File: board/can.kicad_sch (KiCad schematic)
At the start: 21 parts, among them U4 ATA6561, U5 ATA6561, U6 ATA6561

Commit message: Changing CRX and CTX Round 2 :((
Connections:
- net CANRX7 renamed CANRX3
- net CANTX7 renamed CANTX3
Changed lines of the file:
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@@
 		)
 	)
-	(hierarchical_label "CANTX7"
+	(hierarchical_label "CANTX3"
 		(shape input)
 		(at 81.28 172.72 180)
@@
 		)
 	)
-	(hierarchical_label "CANRX7"
+	(hierarchical_label "CANRX3"
 		(shape output)
 		(at 81.28 175.26 180)

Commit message: Added root pins
Root beer
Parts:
- added C16, C17: 100nF, symbol Device:C
- added C18: 4.7nF, symbol Device:C
- added Conn5: Molex_SL_02, symbol MRDT_Connectors:Molex_SL_02
- added R24, R25: 60, symbol Device:R_US
- added U7: ATA6561, Package_SO:SOIC-8_3.9x4.9mm_P1.27mm, symbol MRDT_Devices:ATA6561
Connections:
- net +3.3V: now also C16.2, U7.5 (VIO)
- net +5V: now also C17.1, U7.3 (VCC)
- net CANRX1: now also U7.4 (RXD)
- net CANTX1: now also U7.1 (TXD)
- net GND: now also C16.1, C17.2, C18.2, U7.2 (GND), U7.8 (STBY)
- new net: C18.1, R24.2, R25.1
- new net: Conn5.2, R25.2, U7.6 (CANL)
- new net: Conn5.1, R24.1, U7.7 (CANH)

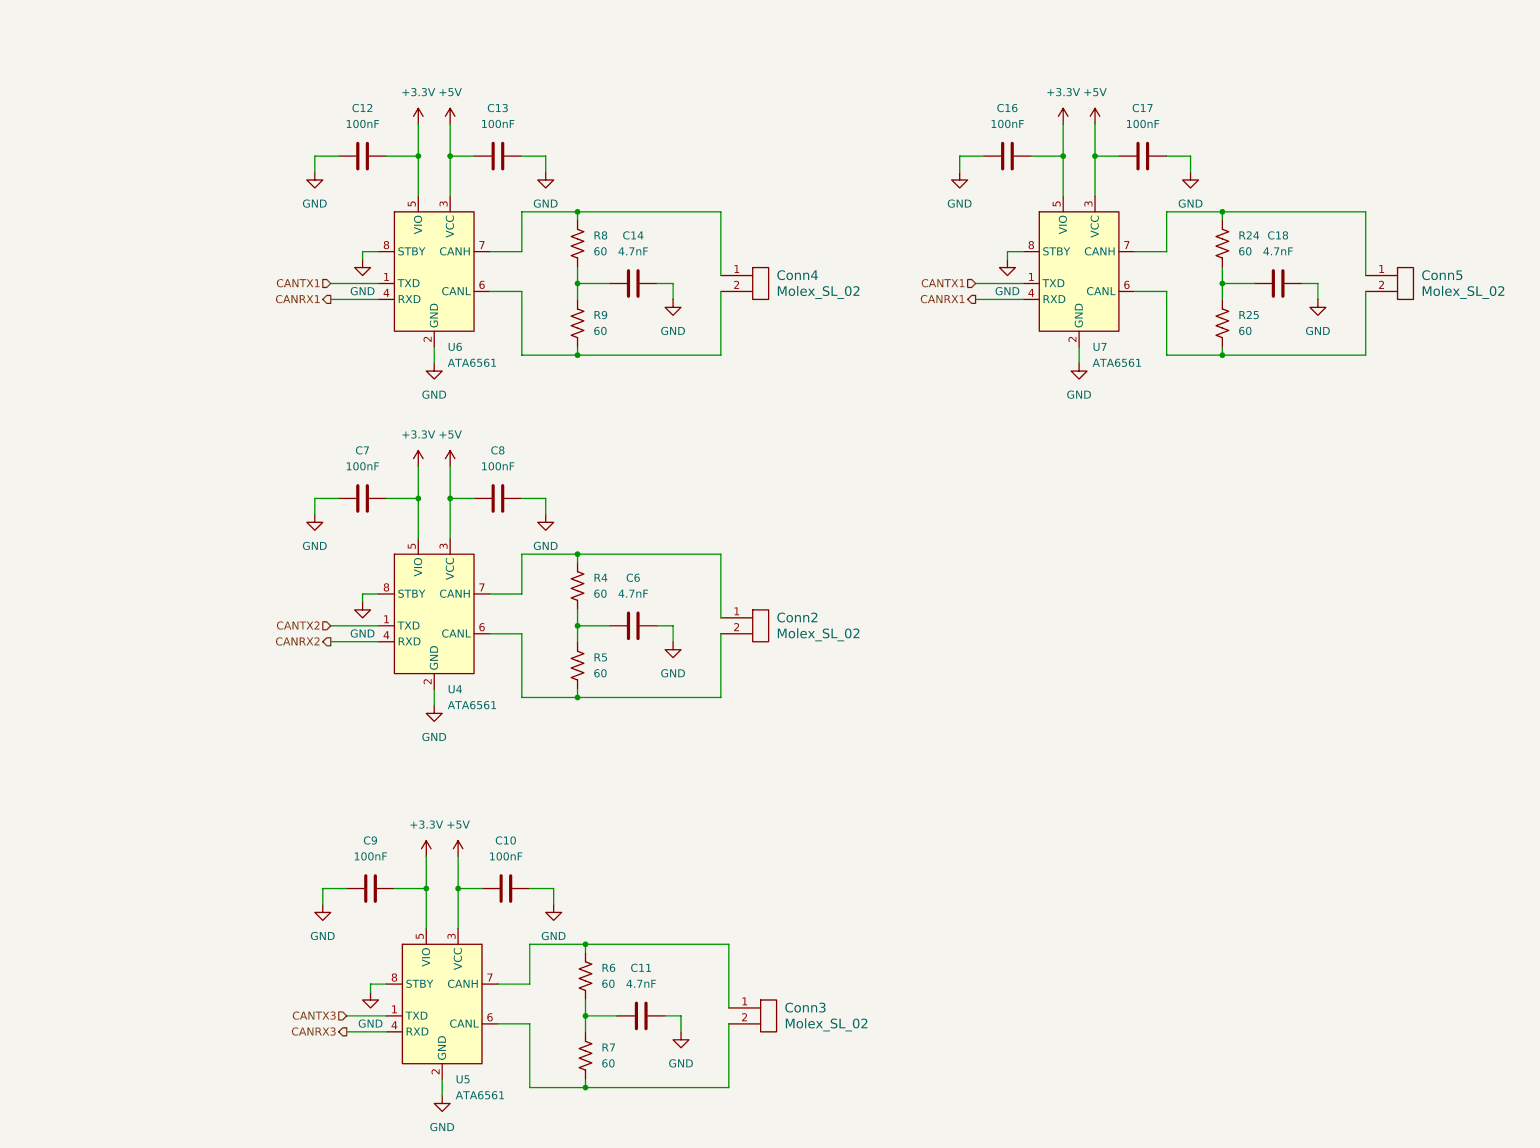
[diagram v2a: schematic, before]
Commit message: Schematic review changes
Updated molex connectors, can ics, buttons are no longer pull ups, and some appearence changes.
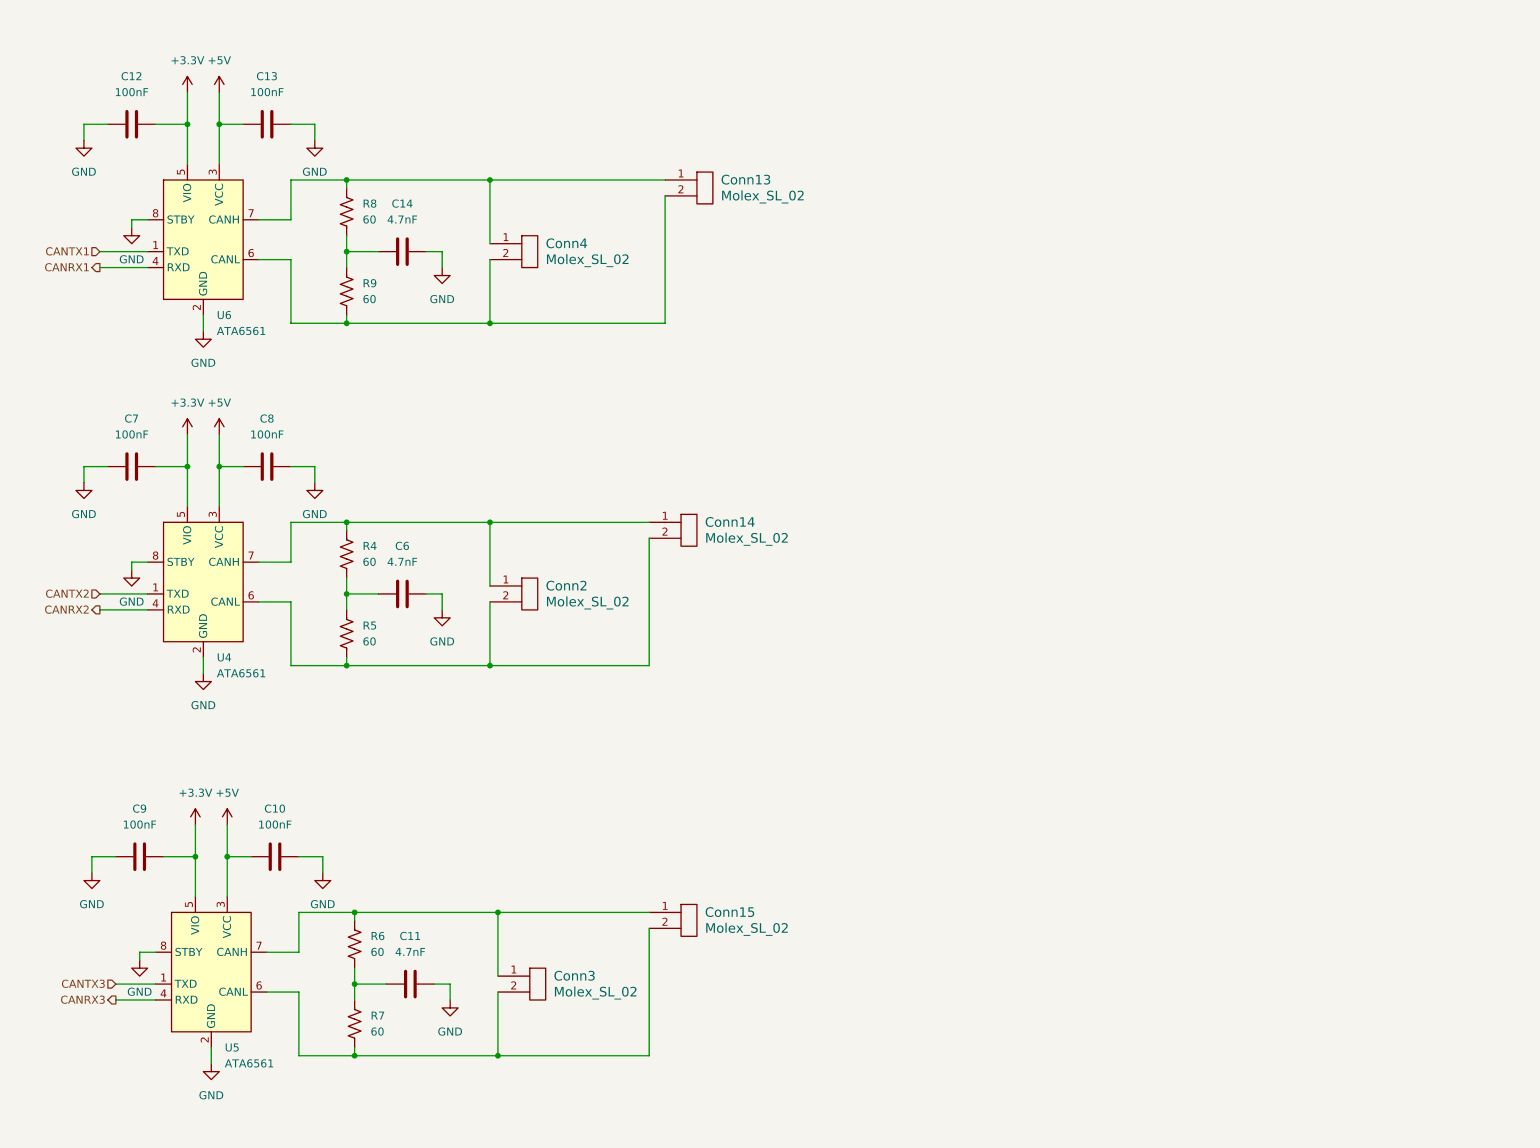
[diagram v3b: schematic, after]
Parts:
- removed C16, C17: 100nF, symbol Device:C
- removed C18: 4.7nF, symbol Device:C
- removed Conn5: Molex_SL_02, symbol MRDT_Connectors:Molex_SL_02
- removed R24, R25: 60, symbol Device:R_US
- removed U7: ATA6561, Package_SO:SOIC-8_3.9x4.9mm_P1.27mm, symbol MRDT_Devices:ATA6561
- added Conn13, Conn14, Conn15: Molex_SL_02, symbol MRDT_Connectors:Molex_SL_02
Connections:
- net at Conn4.2, R9.2, U6.6 (CANL): now also Conn13.2
- net at Conn2.1, R4.1, U4.7 (CANH): now also Conn14.1
- net at Conn2.2, R5.2, U4.6 (CANL): now also Conn14.2
- net at Conn4.1, R8.1, U6.7 (CANH): now also Conn13.1
- net at Conn3.1, R6.1, U5.7 (CANH): now also Conn15.1
- net at Conn3.2, R7.2, U5.6 (CANL): now also Conn15.2
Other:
- moved on the sheet: C10, C11, C12, C13, C14, C6, C7, C8, C9, Conn2, Conn3, Conn4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

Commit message: Prototype Layout
Made an initial Layout to be edited and changed uwu
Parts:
- C10, C11, C12, C13, C14, C6, C7, C8, C9: footprint (none) -> Capacitor_SMD:C_0603_1608Metric_Pad1.08x0.95mm_HandSolder
- Conn13, Conn14, Conn15, Conn2, Conn3, Conn4: footprint (none) -> MRDT_Connectors:MOLEX_SL_02_Vertical
- R4, R5, R6, R7, R8, R9: footprint (none) -> Resistor_SMD:R_0603_1608Metric_Pad0.98x0.95mm_HandSolder
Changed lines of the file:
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@@
 			)
 		)
-		(property "Footprint" ""
+		(property "Footprint" "Capacitor_SMD:C_0603_1608Metric_Pad1.08x0.95mm_HandSolder"
 			(at 73.66 146.3548 0)
 			(effects
@@
 			)
 		)
-		(property "Footprint" ""
+		(property "Footprint" "Resistor_SMD:R_0603_1608Metric_Pad0.98x0.95mm_HandSolder"
 			(at 82.296 57.404 90)
 			(effects
@@
 			)
 		)
-		(property "Footprint" ""
+		(property "Footprint" "Capacitor_SMD:C_0603_1608Metric_Pad1.08x0.95mm_HandSolder"
 			(at 72.39 84.1248 0)
 			(effects
@@
 			)
 		)
-		(property "Footprint" ""
+		(property "Footprint" "MRDT_Connectors:MOLEX_SL_02_Vertical"
 			(at 137.16 45.72 0)
 			(effects
@@
 			)
 		)
-		(property "Footprint" ""
+		(property "Footprint" "Resistor_SMD:R_0603_1608Metric_Pad0.98x0.95mm_HandSolder"
 			(at 82.296 99.314 90)
 			(effects
@@
 			)
 		)
-		(property "Footprint" ""
+		(property "Footprint" "MRDT_Connectors:MOLEX_SL_02_Vertical"
 			(at 109.22 110.49 0)
 			(effects
@@
 			)
 		)
-		(property "Footprint" ""
+		(property "Footprint" "Capacitor_SMD:C_0603_1608Metric_Pad1.08x0.95mm_HandSolder"
 			(at 93.98 49.8348 0)
 			(effects
@@
 			)
 		)
-		(property "Footprint" ""
+		(property "Footprint" "MRDT_Connectors:MOLEX_SL_02_Vertical"
 			(at 109.22 55.88 0)
 			(effects
@@
 			)
 		)
-		(property "Footprint" ""
+		(property "Footprint" "Capacitor_SMD:C_0603_1608Metric_Pad1.08x0.95mm_HandSolder"
 			(at 95.25 166.6748 0)
 			(effects
@@
 			)
 		)
-		(property "Footprint" ""
+		(property "Footprint" "Capacitor_SMD:C_0603_1608Metric_Pad1.08x0.95mm_HandSolder"
 			(at 52.07 146.3548 0)
 			(effects
@@
 			)
 		)
-		(property "Footprint" ""
+		(property "Footprint" "Capacitor_SMD:C_0603_1608Metric_Pad1.08x0.95mm_HandSolder"
 			(at 72.39 29.5148 0)
 			(effects
@@
 			)
 		)
-		(property "Footprint" ""
+		(property "Footprint" "Resistor_SMD:R_0603_1608Metric_Pad0.98x0.95mm_HandSolder"
 			(at 83.566 161.544 90)
 			(effects
@@
 			)
 		)
-		(property "Footprint" ""
+		(property "Footprint" "MRDT_Connectors:MOLEX_SL_02_Vertical"
 			(at 134.62 162.56 0)
 			(effects
@@
 			)
 		)
-		(property "Footprint" ""
+		(property "Footprint" "Resistor_SMD:R_0603_1608Metric_Pad0.98x0.95mm_HandSolder"
 			(at 82.296 44.704 90)
 			(effects
@@
 			)
 		)
-		(property "Footprint" ""
+		(property "Footprint" "Capacitor_SMD:C_0603_1608Metric_Pad1.08x0.95mm_HandSolder"
 			(at 50.8 29.5148 0)
 			(effects
@@
 			)
 		)
-		(property "Footprint" ""
+		(property "Footprint" "Capacitor_SMD:C_0603_1608Metric_Pad1.08x0.95mm_HandSolder"
 			(at 50.8 84.1248 0)
 			(effects
@@
 			)
 		)
-		(property "Footprint" ""
+		(property "Footprint" "MRDT_Connectors:MOLEX_SL_02_Vertical"
 			(at 134.62 100.33 0)
 			(effects
@@
 			)
 		)
-		(property "Footprint" ""
+		(property "Footprint" "Resistor_SMD:R_0603_1608Metric_Pad0.98x0.95mm_HandSolder"
 			(at 82.296 112.014 90)
 			(effects
@@
 			)
 		)
-		(property "Footprint" ""
+		(property "Footprint" "Capacitor_SMD:C_0603_1608Metric_Pad1.08x0.95mm_HandSolder"
 			(at 93.98 104.4448 0)
 			(effects
@@
 			)
 		)
-		(property "Footprint" ""
+		(property "Footprint" "MRDT_Connectors:MOLEX_SL_02_Vertical"
 			(at 110.49 172.72 0)
 			(effects
@@
 			)
 		)
-		(property "Footprint" ""
+		(property "Footprint" "Resistor_SMD:R_0603_1608Metric_Pad0.98x0.95mm_HandSolder"
 			(at 83.566 174.244 90)
 			(effects

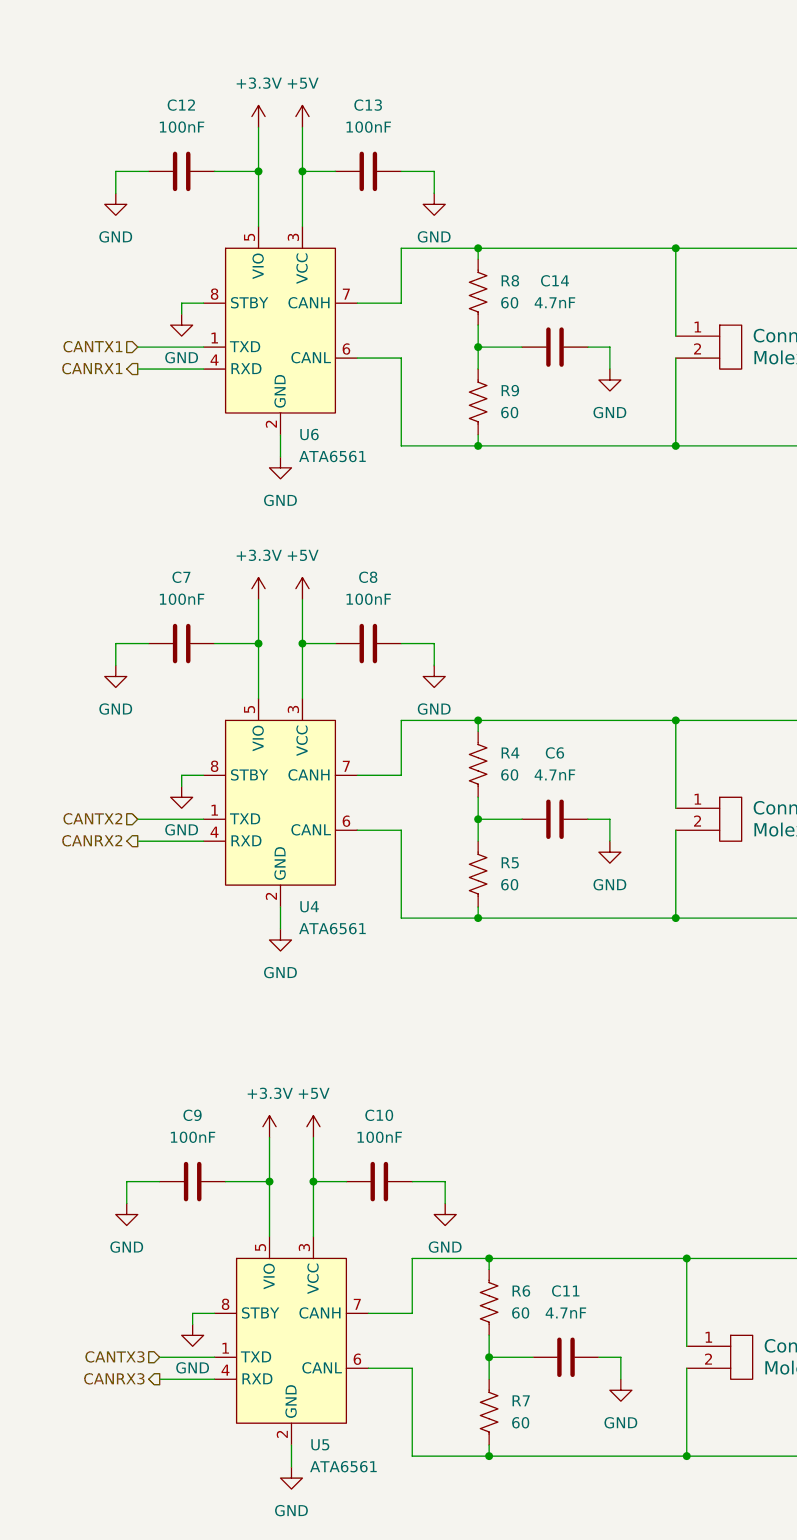
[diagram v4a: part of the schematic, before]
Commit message: Rev 2 start
Fixed schematic for Rev 2, needs layout changes see sharepoint
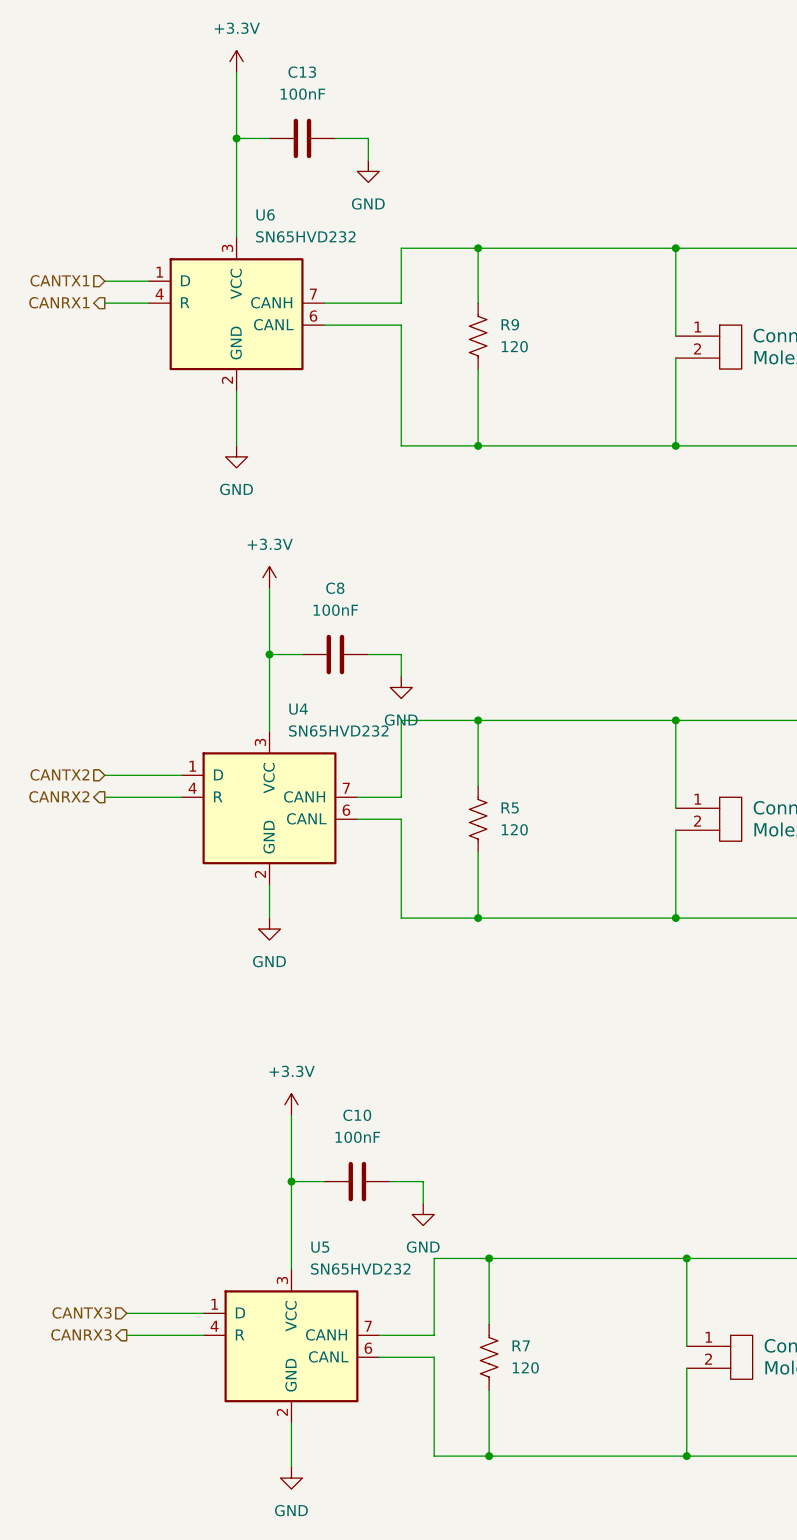
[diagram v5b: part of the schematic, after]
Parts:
- removed C11, C14, C6: 4.7nF, Capacitor_SMD:C_0603_1608Metric_Pad1.08x0.95mm_HandSolder, symbol Device:C
- removed C12, C7, C9: 100nF, Capacitor_SMD:C_0603_1608Metric_Pad1.08x0.95mm_HandSolder, symbol Device:C
- removed R4, R6, R8: 60, Resistor_SMD:R_0603_1608Metric_Pad0.98x0.95mm_HandSolder, symbol Device:R_US
- removed U4, U5, U6: ATA6561, Package_SO:SOIC-8_3.9x4.9mm_P1.27mm, symbol MRDT_Devices:ATA6561
- added U4, U5, U6: SN65HVD232, Package_SO:SOIC-8_3.9x4.9mm_P1.27mm, symbol Interface_CAN_LIN:SN65HVD232
- R5, R7, R9: value 60 -> 120
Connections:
- net +5V is gone; now on net +3.3V: C10.1, C13.1, C8.1
- net +3.3V: now also U4.3 (VCC), U5.3 (VCC), U6.3 (VCC)
- net CANRX1: now also U6.4 (R)
- net CANRX2: now also U4.4 (R)
- net CANRX3: now also U5.4 (R)
- net CANTX1: now also U6.1 (D)
- net CANTX2: now also U4.1 (D)
- net CANTX3: now also U5.1 (D)
- net GND: now also U4.2 (GND), U5.2 (GND), U6.2 (GND)
- net at R9.1: now also Conn13.1, Conn4.1, U6.7 (CANH)
- net at Conn13.2, Conn4.2, R9.2: now also U6.6 (CANL)
- net at Conn14.1, Conn2.1: now also R5.1, U4.7 (CANH)
- net at Conn14.2, Conn2.2, R5.2: now also U4.6 (CANL)
- net at R7.1: now also Conn15.1, Conn3.1, U5.7 (CANH)
- net at Conn15.2, Conn3.2, R7.2: now also U5.6 (CANL)
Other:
- moved on the sheet: C10, C13, C8, R5, R7, R9
